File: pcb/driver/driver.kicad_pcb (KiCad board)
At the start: 2 copper layers, 99 x 34 mm, 17 parts, among them J2 Conn_01x05_Male, U10 MAX7219, U11 LED_MATRIX, U12 MAX7219, U13 LED_MATRIX, U14 LED_MATRIX, U5 MAX7219, U8 MAX7219, U9 LED_MATRIX

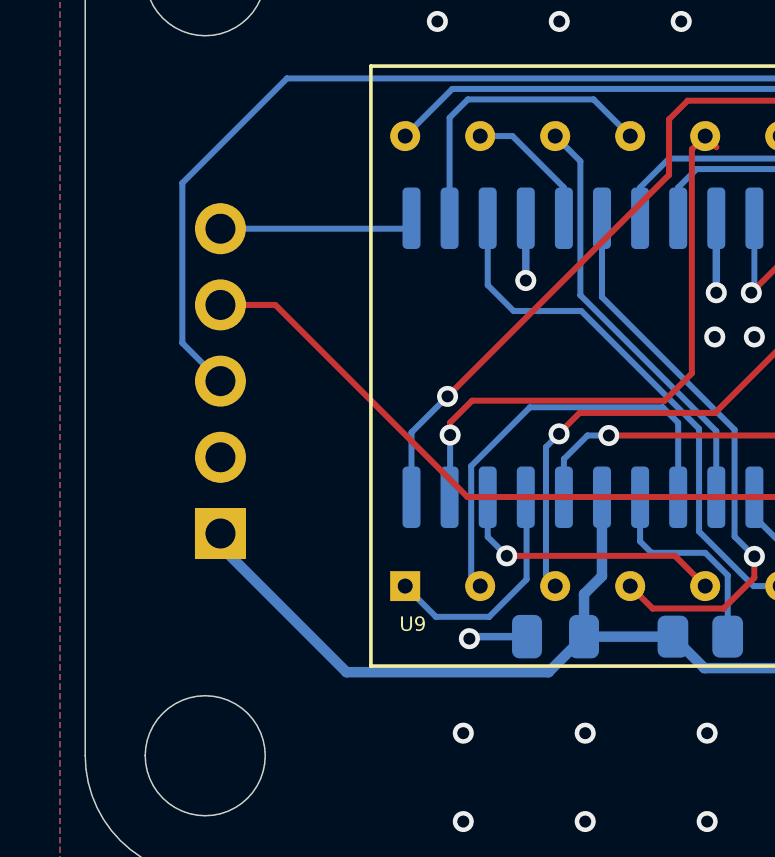
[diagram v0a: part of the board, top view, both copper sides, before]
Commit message: PCB调整 3D装配图
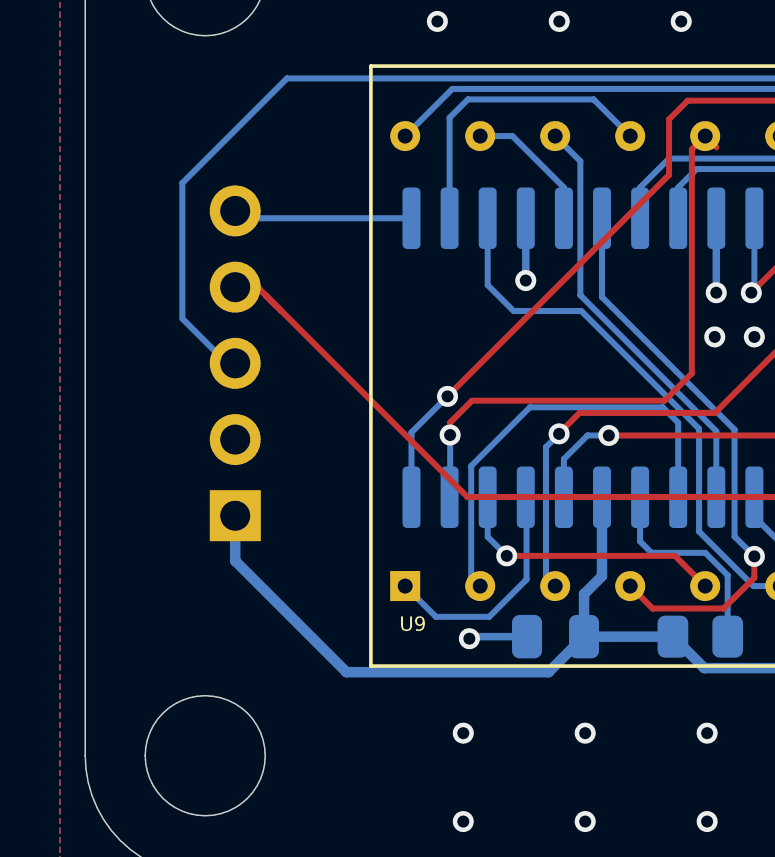
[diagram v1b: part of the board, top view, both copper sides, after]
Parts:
- moved J2 0.77 mm to (36.3, 54.5)
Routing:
- net /SPI_MOSI: track 6.80 -> 5.98 mm
